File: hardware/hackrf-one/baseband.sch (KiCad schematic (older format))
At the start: 123 parts, among them P10 TXBBI, P11 RXBBI, P12 RXBBQ, P14 XCVR_CLKOUT, P15 INTR, P16 CLKIN, P18 OEB, P2 CLKOUT, P36 VAA, P37 SCL, P38 SDA, P39 SSP1_SCK, P40 SSP1_MOSI, P41 SSP1_MISO, P53 CS_XCVR, P54 CS_AD, P55 TXENABLE, P56 RXENABLE, P57 XTAL2, P58 GCK1, P59 GCK2, P60 SGPIO_CLK, P61 DA0, P62 DA7, P63 DD0, P64 DD9, P65 DA4, P66 DD5, P67 RSSI, P9 TXBBQ, Q3 MOSFET_P, T3 RX_BALUN, T4 TX_BALUN, U17 MAX2837, U18 MAX5864, U19 SI5351C, X1 GSG-XTAL4PIN

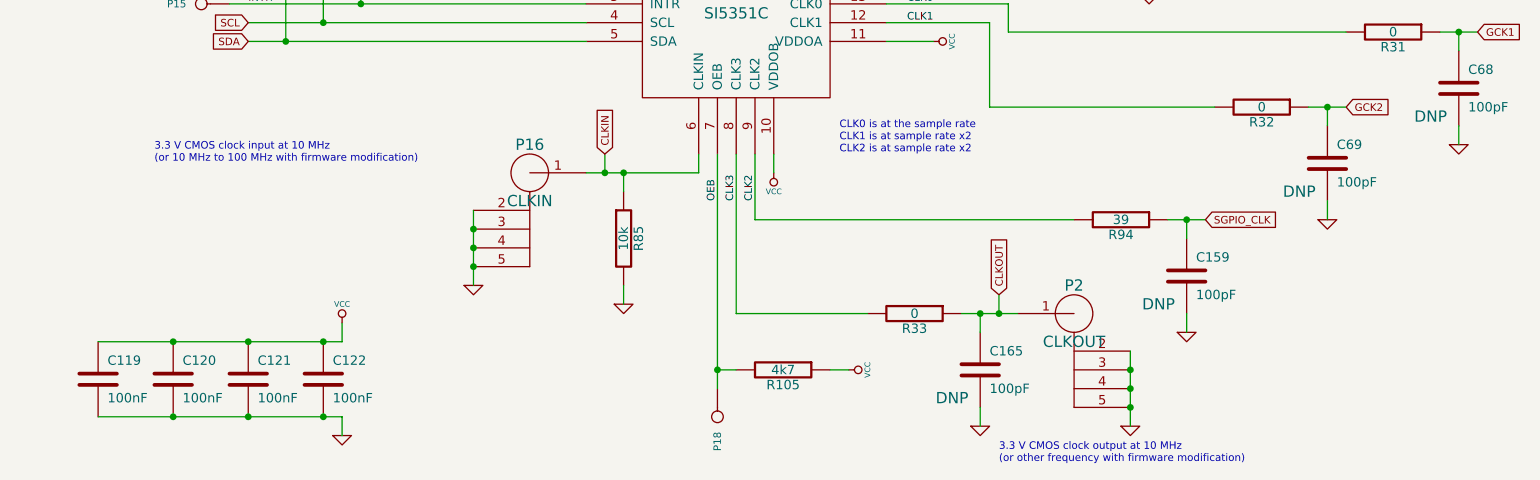
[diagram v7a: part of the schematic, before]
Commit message: TVS diodes for CLKIN and CLKOUT
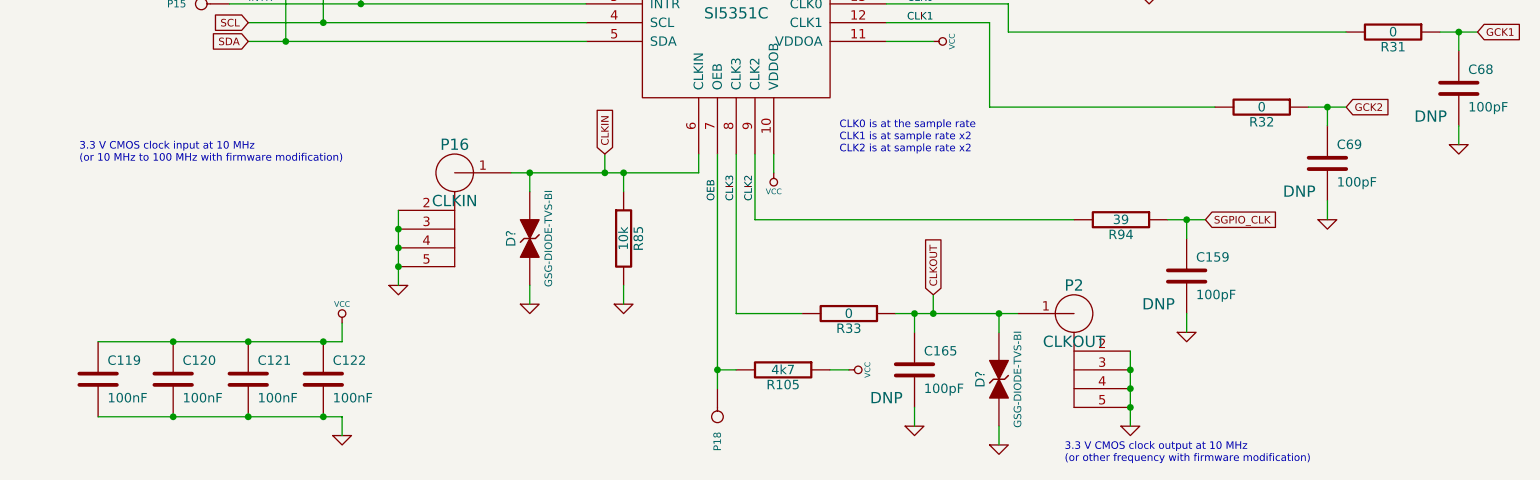
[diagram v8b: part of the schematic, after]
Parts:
- added D? (x2): GSG-DIODE-TVS-BI, symbol GSG-DIODE-TVS-BI
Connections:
- net CLKIN: now also D?.2 (K)
- net CLKOUT: now also D?.2 (K)
- net GND: now also D?.1 (A), D?.1 (A)
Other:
- moved on the sheet: C165, P16, R33
